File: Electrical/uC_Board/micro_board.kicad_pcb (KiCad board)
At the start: 2 copper layers, 45 x 18 mm, 27 parts, among them J1 card_edge_6p, SW1 SW_Push, U1 ATmega328PB-AU, U2 ArdStripNano, U3 CSTNE16M0V530000R0, U4 AD8620, U5 LM1117MPX-5.0

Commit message: updated BOM
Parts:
- R2, U3: moved to B.Cu
- moved U3 35.1 mm to (129.8, 103.0), turned to 180 degrees
- moved R2 25.2 mm to (127.5, 99.0), turned to 180 degrees
- moved C2 13.6 mm to (121.8, 103.8), turned to 225 degrees
- moved C3 11.7 mm to (120.5, 102.5)
- moved C1 11.5 mm to (123.0, 105.0)
- moved R1 7.89 mm to (127.5, 97.2)
- moved D2 0.56 mm to (140.0, 105.0)
- moved J1 0.50 mm to (102.2, 105.0)
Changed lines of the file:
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@@
   (general
     (thickness 1.6)
-    (drawings 11)
+    (drawings 9)
     (tracks 0)
     (zones 0)
@@
     (46 B.CrtYd user)
     (47 F.CrtYd user)
-    (48 B.Fab user)
-    (49 F.Fab user)
+    (48 B.Fab user hide)
+    (49 F.Fab user hide)
   )
   (setup
@@
     (solder_mask_min_width 0.25)
     (aux_axis_origin 0 0)
-    (visible_elements 7FFFFFFF)
+    (visible_elements 7FFFF7FF)
     (pcbplotparams
       (layerselection 0x010fc_ffffffff)
@@
   )
   (module hodgkin:card_edge_6p_single_side (layer F.Cu)
-    (at 101.75 105 90)
+    (at 102.25 105 90)
     (fp_text reference J1 (at 6.604 -2.032 90) (layer F.SilkS)
       (effects (font (size 1 1) (thickness 0.15)))
@@
     )
   )
-  (module hodgkin:CSTNE16M0V530000R0 (layer F.Cu)
-    (at 162.964999 91.613)
-    (fp_text reference U3 (at -1.802999 -0.285) (layer F.SilkS)
-      (effects (font (size 1 1) (thickness 0.15)))
-    )
-    (fp_text value CSTNE16M0V530000R0 (at -17.78 -5.08) (layer F.Fab)
-      (effects (font (size 1 1) (thickness 0.15)))
-    )
-    (fp_line (start 0 -1.3) (end 0 0) (layer F.SilkS) (width 0.15))
-    (fp_line (start 3.2 -1.3) (end 0 -1.3) (layer F.SilkS) (width 0.15))
-    (fp_line (start 3.2 0) (end 3.2 -1.3) (layer F.SilkS) (width 0.15))
-    (fp_line (start 0 0) (end 3.2 0) (layer F.SilkS) (width 0.15))
-    (pad 3 smd rect (at 2.8 -0.65) (size 0.4 1.3) (layers F.Cu F.Paste F.Mask)
-      (net 1 GND))
-    (pad 2 smd rect (at 1.6 -0.65) (size 0.4 1.3) (layers F.Cu F.Paste F.Mask)
+  (module hodgkin:CSTNE16M0V530000R0 (layer B.Cu)
+    (at 129.75 103 180)
+    (fp_text reference U3 (at -1.802999 0.285) (layer B.SilkS)
+      (effects (font (size 1 1) (thickness 0.15)) (justify mirror))
+    )
+    (fp_text value CSTNE16M0V530000R0 (at -17.78 5.08) (layer B.Fab)
+      (effects (font (size 1 1) (thickness 0.15)) (justify mirror))
+    )
+    (fp_line (start 0 1.3) (end 0 0) (layer B.SilkS) (width 0.15))
+    (fp_line (start 3.2 1.3) (end 0 1.3) (layer B.SilkS) (width 0.15))
+    (fp_line (start 3.2 0) (end 3.2 1.3) (layer B.SilkS) (width 0.15))
+    (fp_line (start 0 0) (end 3.2 0) (layer B.SilkS) (width 0.15))
+    (pad 3 smd rect (at 2.8 0.65 180) (size 0.4 1.3) (layers B.Cu B.Paste B.Mask)
+      (net 1 GND))
+    (pad 2 smd rect (at 1.6 0.65 180) (size 0.4 1.3) (layers B.Cu B.Paste B.Mask)
       (net 32 "Net-(U1-Pad7)"))
-    (pad 1 smd rect (at 0.4 -0.65) (size 0.4 1.3) (layers F.Cu F.Paste F.Mask)
+    (pad 1 smd rect (at 0.4 0.65 180) (size 0.4 1.3) (layers B.Cu B.Paste B.Mask)
       (net 31 "Net-(U1-Pad8)"))
   )
@@
     )
   )
-  (module Resistors_SMD:R_0603 (layer F.Cu)
-    (at 143.573 79.641 270)
+  (module Resistors_SMD:R_0603 (layer B.Cu)
+    (at 127.5 99 180)
     (descr "Resistor SMD 0603, reflow soldering, Vishay (see dcrcw.pdf)")
     (tags "resistor 0603")
     (attr smd)
-    (fp_text reference R2 (at 0 -1.45 90) (layer F.SilkS)
-      (effects (font (size 1 1) (thickness 0.15)))
-    )
-    (fp_text value 1k (at 0 1.5 90) (layer F.Fab)
-      (effects (font (size 1 1) (thickness 0.15)))
-    )
-    (fp_text user %R (at 0 0 90) (layer F.Fab)
-      (effects (font (size 0.4 0.4) (thickness 0.075)))
-    )
-    (fp_line (start -0.8 0.4) (end -0.8 -0.4) (layer F.Fab) (width 0.1))
-    (fp_line (start 0.8 0.4) (end -0.8 0.4) (layer F.Fab) (width 0.1))
-    (fp_line (start 0.8 -0.4) (end 0.8 0.4) (layer F.Fab) (width 0.1))
-    (fp_line (start -0.8 -0.4) (end 0.8 -0.4) (layer F.Fab) (width 0.1))
-    (fp_line (start 0.5 0.68) (end -0.5 0.68) (layer F.SilkS) (width 0.12))
-    (fp_line (start -0.5 -0.68) (end 0.5 -0.68) (layer F.SilkS) (width 0.12))
-    (fp_line (start -1.25 -0.7) (end 1.25 -0.7) (layer F.CrtYd) (width 0.05))
-    (fp_line (start -1.25 -0.7) (end -1.25 0.7) (layer F.CrtYd) (width 0.05))
-    (fp_line (start 1.25 0.7) (end 1.25 -0.7) (layer F.CrtYd) (width 0.05))
-    (fp_line (start 1.25 0.7) (end -1.25 0.7) (layer F.CrtYd) (width 0.05))
-    (pad 1 smd rect (at -0.75 0 270) (size 0.5 0.9) (layers F.Cu F.Paste F.Mask)
+    (fp_text reference R2 (at 0 1.45 180) (layer B.SilkS)
+      (effects (font (size 1 1) (thickness 0.15)) (justify mirror))
+    )
+    (fp_text value 1k (at 0 -1.5 180) (layer B.Fab)
+      (effects (font (size 1 1) (thickness 0.15)) (justify mirror))
+    )
+    (fp_text user %R (at 0 0 180) (layer B.Fab)
+      (effects (font (size 0.4 0.4) (thickness 0.075)) (justify mirror))
+    )
+    (fp_line (start -0.8 -0.4) (end -0.8 0.4) (layer B.Fab) (width 0.1))
+    (fp_line (start 0.8 -0.4) (end -0.8 -0.4) (layer B.Fab) (width 0.1))
+    (fp_line (start 0.8 0.4) (end 0.8 -0.4) (layer B.Fab) (width 0.1))
+    (fp_line (start -0.8 0.4) (end 0.8 0.4) (layer B.Fab) (width 0.1))
+    (fp_line (start 0.5 -0.68) (end -0.5 -0.68) (layer B.SilkS) (width 0.12))
+    (fp_line (start -0.5 0.68) (end 0.5 0.68) (layer B.SilkS) (width 0.12))
+    (fp_line (start -1.25 0.7) (end 1.25 0.7) (layer B.CrtYd) (width 0.05))
+    (fp_line (start -1.25 0.7) (end -1.25 -0.7) (layer B.CrtYd) (width 0.05))
+    (fp_line (start 1.25 -0.7) (end 1.25 0.7) (layer B.CrtYd) (width 0.05))
+    (fp_line (start 1.25 -0.7) (end -1.25 -0.7) (layer B.CrtYd) (width 0.05))
+    (pad 1 smd rect (at -0.75 0 180) (size 0.5 0.9) (layers B.Cu B.Paste B.Mask)
       (net 14 /TX))
-    (pad 2 smd rect (at 0.75 0 270) (size 0.5 0.9) (layers F.Cu F.Paste F.Mask)
+    (pad 2 smd rect (at 0.75 0 180) (size 0.5 0.9) (layers B.Cu B.Paste B.Mask)
       (net 15 /D1))
     (model ${KISYS3DMOD}/Resistors_SMD.3dshapes/R_0603.wrl
@@
   )
   (module Resistors_SMD:R_0603 (layer B.Cu)
-    (at 135.146 95.293 180)
+    (at 127.5 97.25 180)
     (descr "Resistor SMD 0603, reflow soldering, Vishay (see dcrcw.pdf)")
     (tags "resistor 0603")
@@
   )
   (module Capacitors_SMD:C_0603 (layer B.Cu)
-    (at 121.866 114.128 225)
+    (at 120.5 102.5 225)
     (descr "Capacitor SMD 0603, reflow soldering, AVX (see smccp.pdf)")
     (tags "capacitor 0603")
@@
   )
   (module Capacitors_SMD:C_0805 (layer B.Cu)
-    (at 119.834 117.176)
+    (at 121.75 103.75 225)
     (descr "Capacitor SMD 0805, reflow soldering, AVX (see smccp.pdf)")
     (tags "capacitor 0805")
     (attr smd)
-    (fp_text reference C2 (at 0 1.5) (layer B.SilkS)
-      (effects (font (size 1 1) (thickness 0.15)) (justify mirror))
-    )
-    (fp_text value 4.7uF (at 0 -1.75) (layer B.Fab)
-      (effects (font (size 1 1) (thickness 0.15)) (justify mirror))
-    )
-    (fp_text user %R (at 0 1.5) (layer B.Fab)
+    (fp_text reference C2 (at 0 1.5 45) (layer B.SilkS)
+      (effects (font (size 1 1) (thickness 0.15)) (justify mirror))
+    )
+    (fp_text value 4.7uF (at 0 -1.75 45) (layer B.Fab)
+      (effects (font (size 1 1) (thickness 0.15)) (justify mirror))
+    )
+    (fp_text user %R (at 0 1.5 45) (layer B.Fab)
       (effects (font (size 1 1) (thickness 0.15)) (justify mirror))
     )
@@
     (fp_line (start 1.75 -0.87) (end 1.75 0.88) (layer B.CrtYd) (width 0.05))
     (fp_line (start 1.75 -0.87) (end -1.75 -0.87) (layer B.CrtYd) (width 0.05))
-    (pad 1 smd rect (at -1 0) (size 1 1.25) (layers B.Cu B.Paste B.Mask)
-      (net 9 +5V))
-    (pad 2 smd rect (at 1 0) (size 1 1.25) (layers B.Cu B.Paste B.Mask)
+    (pad 1 smd rect (at -1 0 225) (size 1 1.25) (layers B.Cu B.Paste B.Mask)
+      (net 9 +5V))
+    (pad 2 smd rect (at 1 0 225) (size 1 1.25) (layers B.Cu B.Paste B.Mask)
       (net 1 GND))
     (model Capacitors_SMD.3dshapes/C_0805.wrl
@@
   )
   (module Capacitors_SMD:C_0603 (layer B.Cu)
-    (at 124.406 116.414 225)
+    (at 123 105 225)
     (descr "Capacitor SMD 0603, reflow soldering, AVX (see smccp.pdf)")
     (tags "capacitor 0603")
@@
   )
   (module LEDs:LED_1206 (layer F.Cu)
-    (at 139.5 105.25)
+    (at 140 105)
     (descr "LED 1206 smd package")
     (tags "LED led 1206 SMD smd SMT smt smdled SMDLED smtled SMTLED")
@@
   (gr_line (start 104.7 94.1) (end 100 94.1) (layer Edge.Cuts) (width 0.05))
   (gr_line (start 104.7 91) (end 104.7 94.1) (layer Edge.Cuts) (width 0.05))
-  (gr_line (start 104.7 91) (end 104.7 109) (layer Dwgs.User) (width 0.15))
-  (gr_line (start 100 91) (end 100 109) (layer Dwgs.User) (width 0.15))
   (gr_line (start 94.996 100) (end 152.146 100) (layer Dwgs.User) (width 0.15))
   (gr_line (start 104.7 91) (end 145 91) (layer Edge.Cuts) (width 0.05))

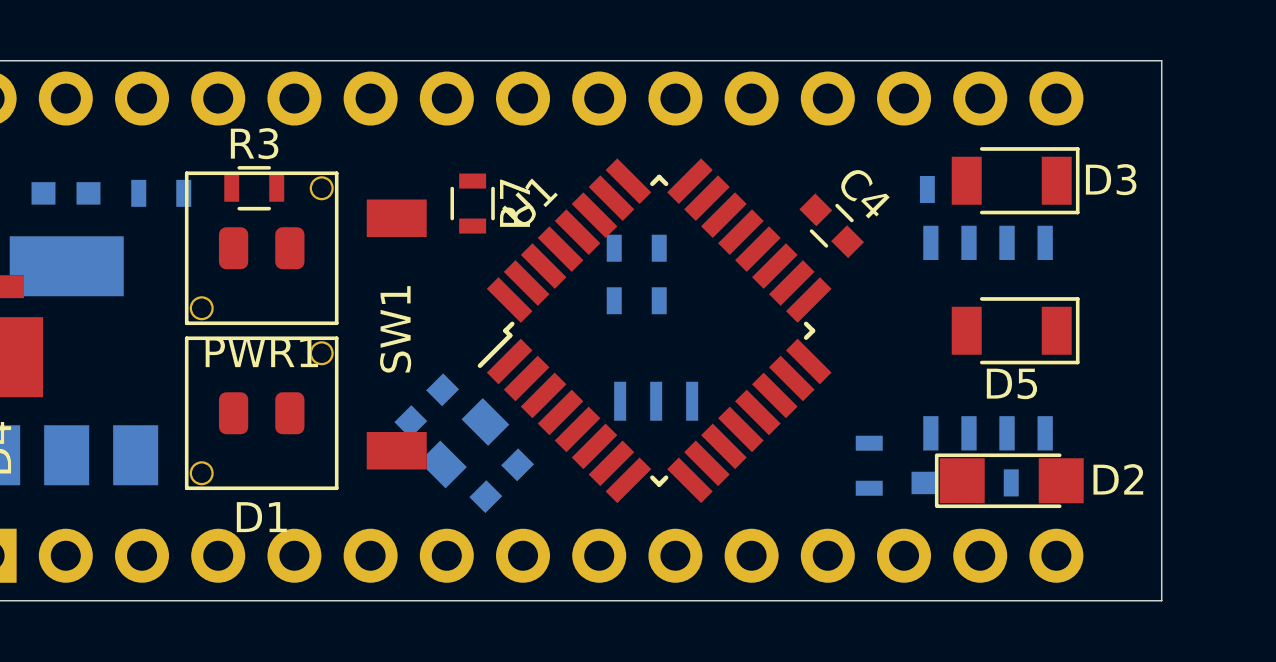
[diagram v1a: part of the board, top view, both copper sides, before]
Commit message: fixed tx connection to have transistor. gave myself a headache trying to figure out a good place to put the atmega
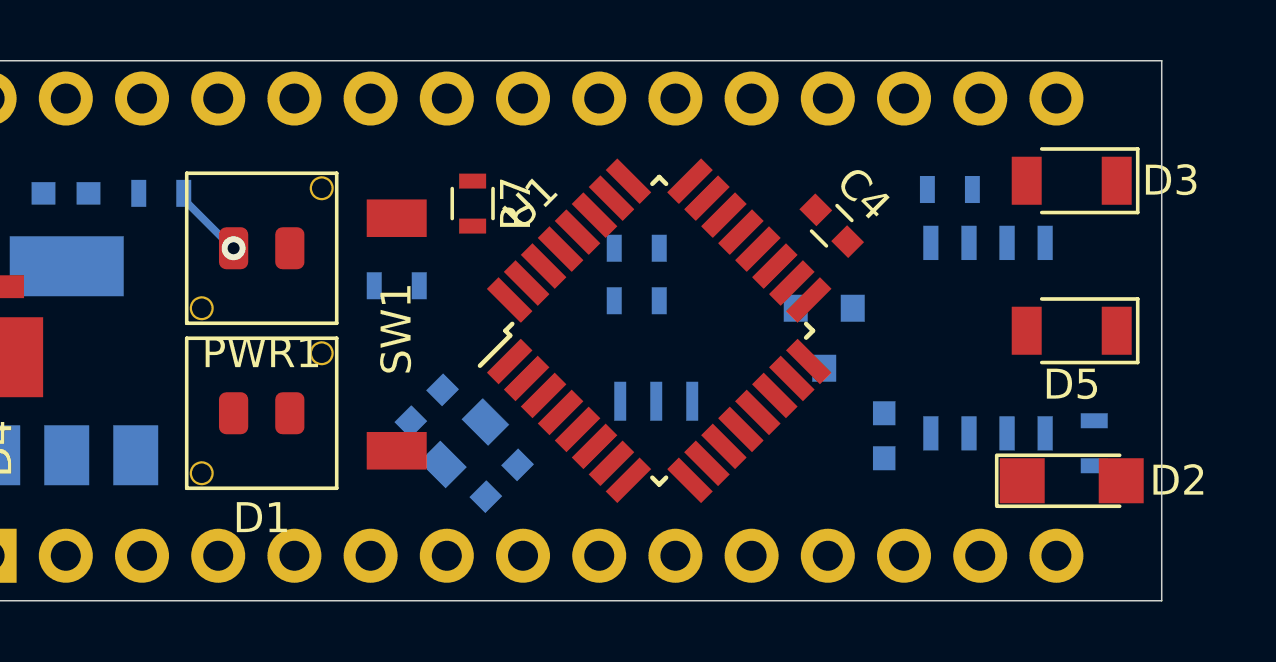
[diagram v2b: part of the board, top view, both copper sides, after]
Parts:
- removed R4: R, Resistors_SMD:R_0603
- added Q1: BC850, TO_SOT_Packages_SMD:SOT-23, B.Cu at (133.8, 100.2)
- R3: moved to B.Cu
- moved R3 5.76 mm to (119.5, 98.5)
- moved C6 2.59 mm to (135.8, 103.5), turned to 90 degrees
- moved R8 2.41 mm to (142.8, 103.8), turned to 90 degrees
- moved D2 2.00 mm to (142.0, 105.0)
- moved D3 2.00 mm to (142.0, 95.0)
- moved D5 2.00 mm to (142.0, 100.0)
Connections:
- D2 pad 1: GND -> Net-(D2-Pad1)
- D2 pad 2: Net-(D2-Pad2) -> +5V
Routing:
- net Net-(PWR1-Pad2): track 0.00 -> 2.54 mm, vias 0 -> 1

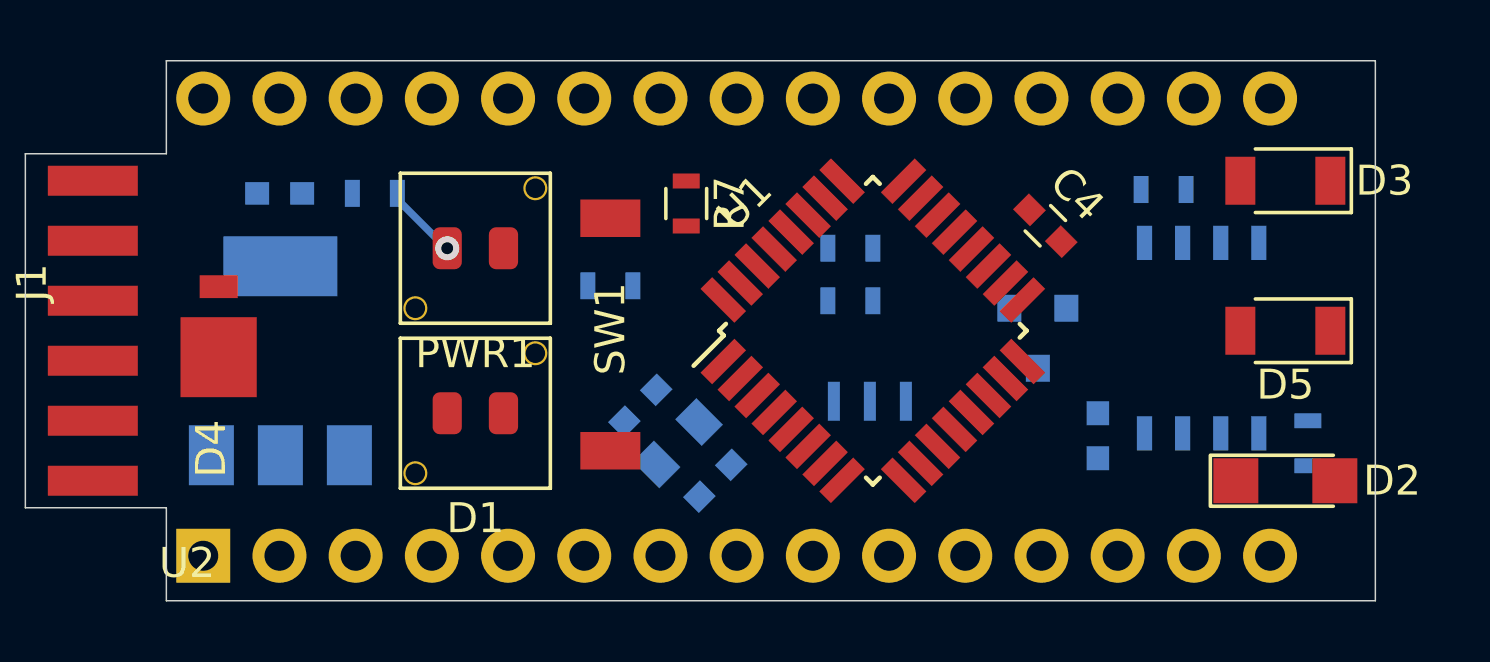
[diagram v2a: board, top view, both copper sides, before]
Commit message: Assisted with uC board component placement.
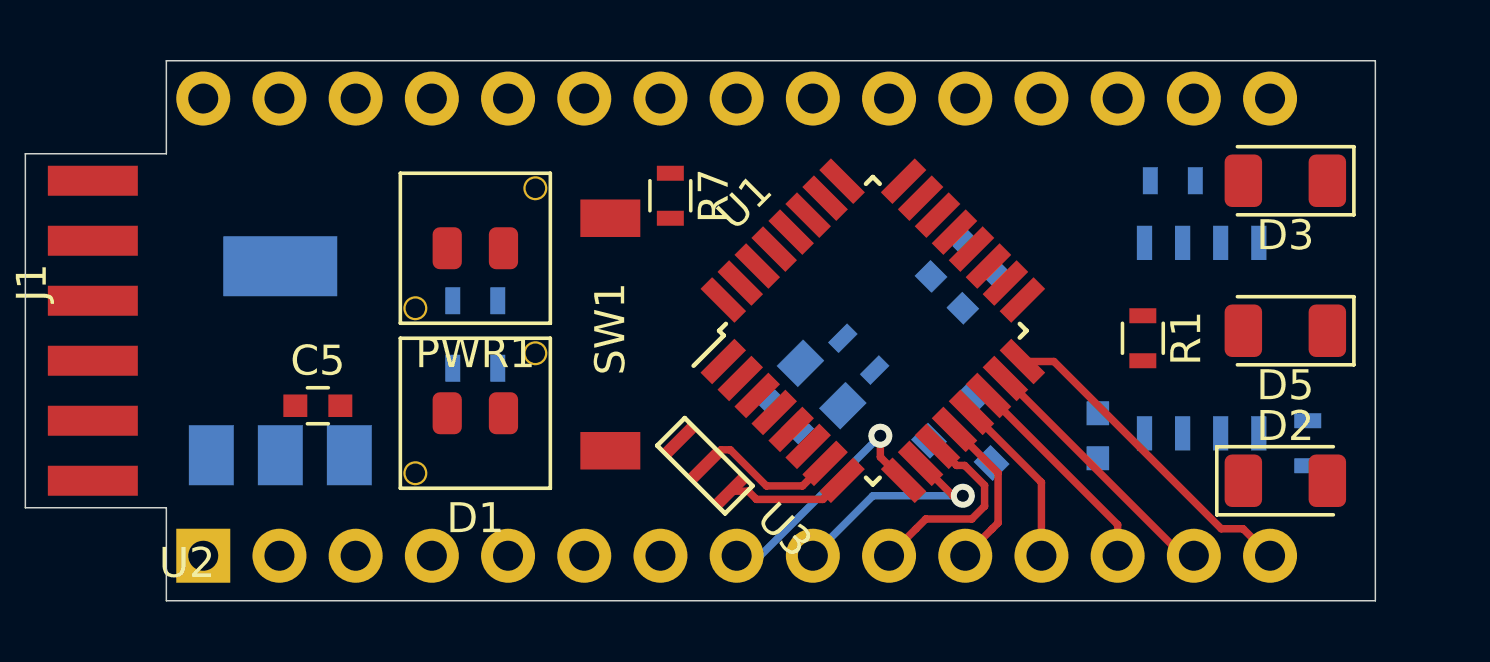
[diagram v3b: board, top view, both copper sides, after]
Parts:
- removed D4: D, hodgkin:DO-220AA-2
- C4: moved to B.Cu
- C5, R1, U3: moved to F.Cu
- D2: footprint LEDs:LED_1206 -> Diode_SMD:D_1206_3216Metric
- D3, D5: footprint Diodes_SMD:D_1206 -> Diode_SMD:D_1206_3216Metric
- moved C3 12.3 mm to (131.7, 97.5), turned to 135 degrees
- moved R1 10.2 mm to (137.2, 100.2), turned to 270 degrees
- moved C5 7.19 mm to (109.8, 102.5)
- moved U3 5.92 mm to (124.2, 105.2), turned to 135 degrees
- moved R3 5.27 mm to (115.0, 101.2)
- moved C2 5.18 mm to (126.5, 101.8), turned to 135 degrees
- moved R6 4.90 mm to (115.0, 99.0), turned to 0 degrees
- moved Q1 4.12 mm to (131.5, 103.7), turned to 315 degrees
- moved C4 3.96 mm to (130.7, 98.7)
- moved C1 3.18 mm to (125.2, 102.7), turned to 315 degrees
- moved R2 1.80 mm to (127.8, 100.8), turned to 135 degrees
- moved R7 0.59 mm to (121.5, 95.5)
- moved R5 0.43 mm to (138.2, 95.0)
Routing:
- net /D12: track 0.00 -> 10.9 mm
- net /D11: track 0.00 -> 8.73 mm
- net /D5: track 0.00 -> 8.25 mm, vias 0 -> 1
- net /D6: track 0.00 -> 7.69 mm, vias 0 -> 1
- net /D10: track 0.00 -> 7.13 mm
- net /D7: track 0.00 -> 6.67 mm
- net /D9: track 0.00 -> 5.74 mm
- net /D8: track 0.00 -> 5.27 mm
- net Net-(U1-Pad7): track 0.00 -> 5.04 mm
- net Net-(U1-Pad8): track 0.00 -> 4.10 mm
- net Net-(PWR1-Pad2): track 2.54 -> 0.03 mm, vias 1 -> 0
